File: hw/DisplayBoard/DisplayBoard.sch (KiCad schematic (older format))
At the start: 29 parts, among them J1 Screw_Terminal_01x02, Q1 2N3906, Q2 2N3906, Q3 2N3906, Q4 2N3906, SW1 SW_Push, SW2 SW_Push, SW3 SW_Push, U1 DS1307+, Y1 32.768 KHz

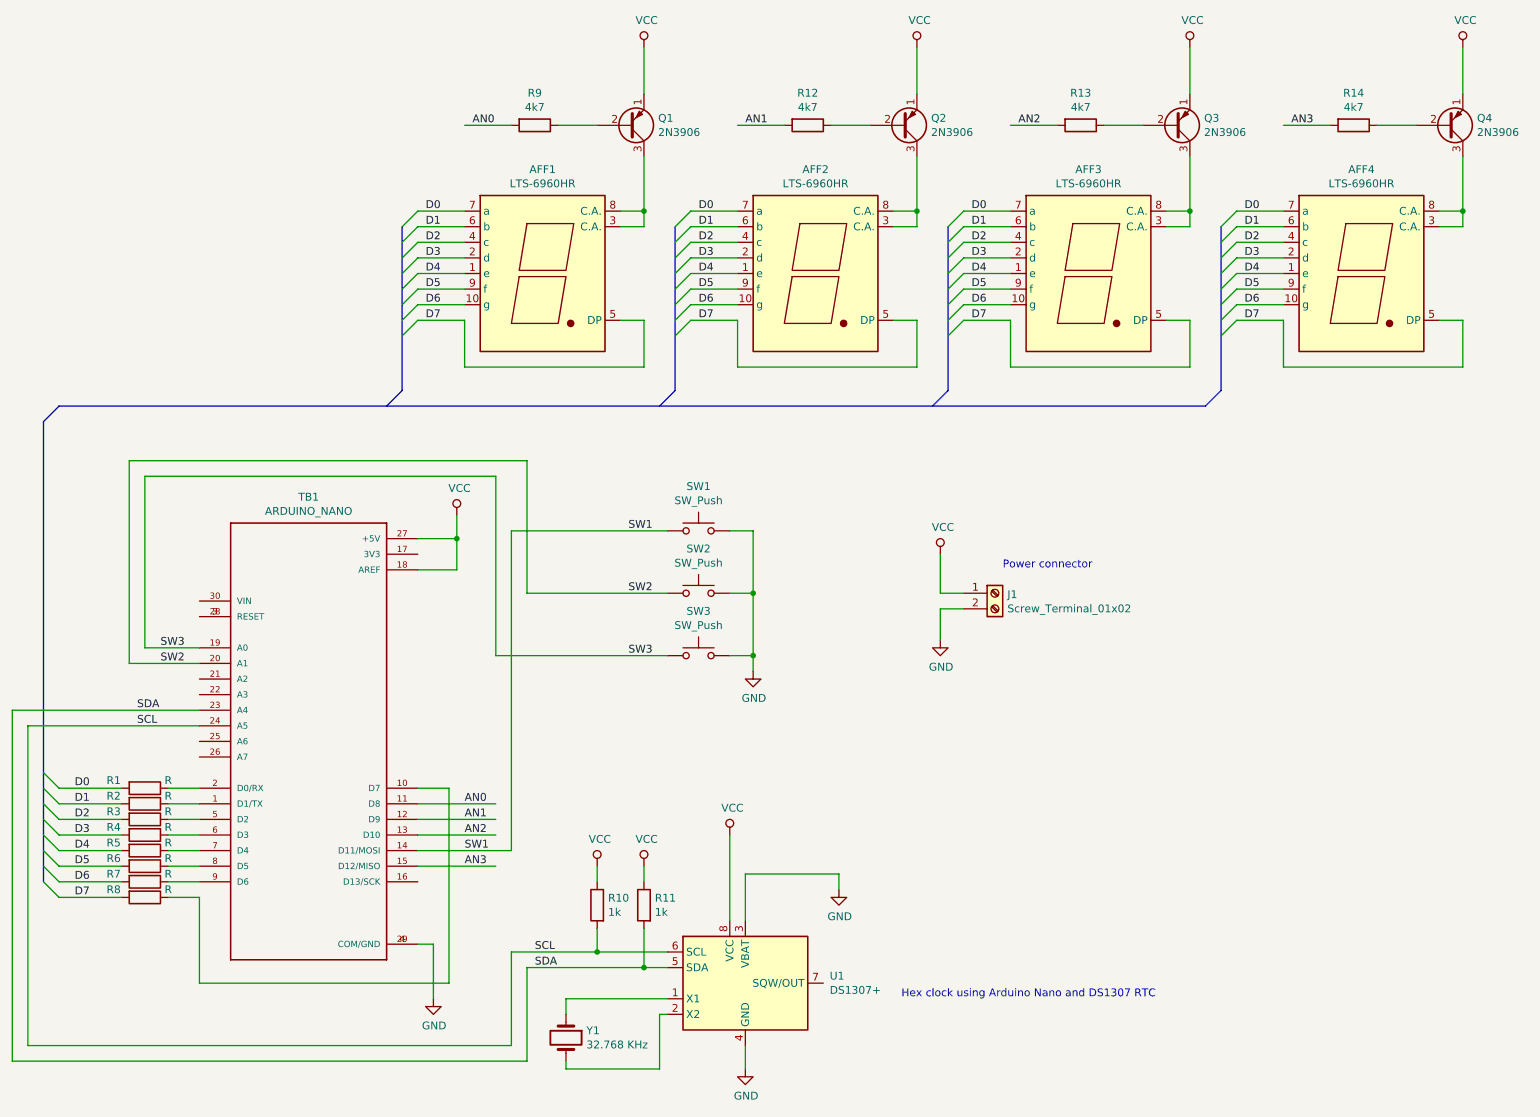
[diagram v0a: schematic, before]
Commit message: edited to make this just the display board
Also, changed to use a 4 digit LED display.
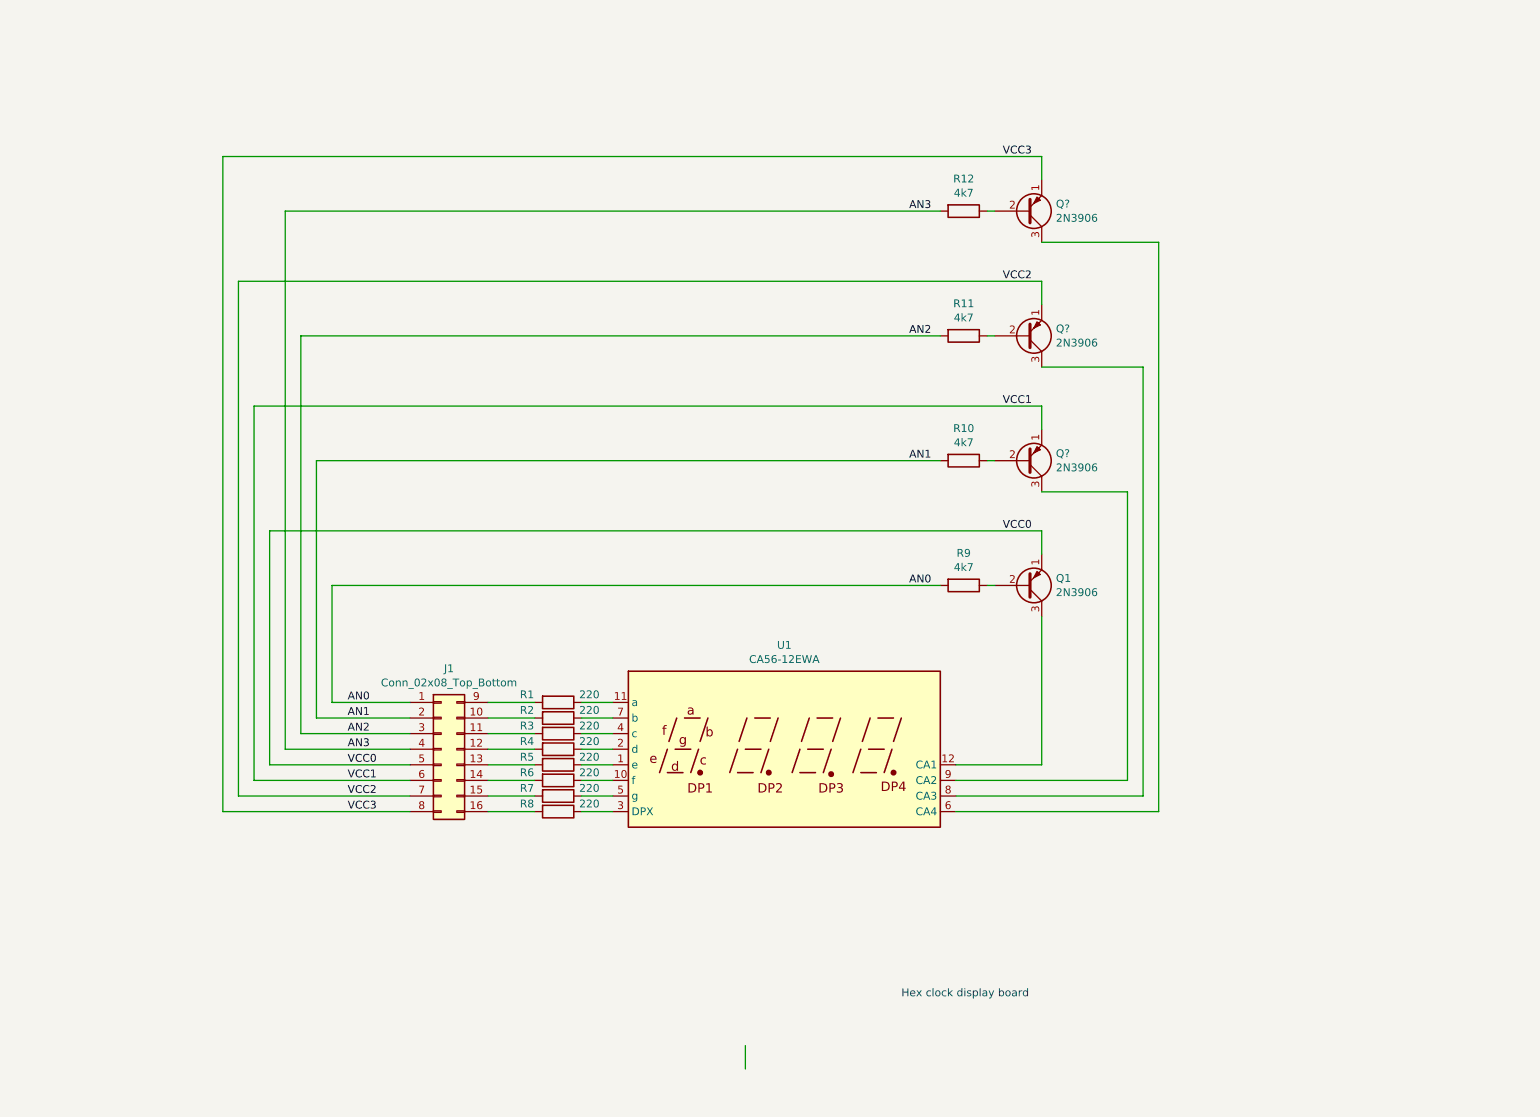
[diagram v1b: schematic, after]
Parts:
- removed AFF1, AFF2, AFF3, AFF4: LTS-6960HR, Display_7Segment:7SegmentLED_LTS6760_LTS6780, symbol Display_Character:LTS-6960HR
- removed J1: Screw_Terminal_01x02, symbol Connector:Screw_Terminal_01x02
- removed Q2, Q3, Q4: 2N3906, symbol device:Q_PNP_EBC
- removed R13, R14: 4k7, symbol device:R
- removed SW1, SW2, SW3: SW_Push, symbol Switch:SW_Push
- removed TB1: ARDUINO_NANO, SHIELD_ARDUINO_NANO, symbol ARDUINO_NANO:ARDUINO_NANO
- removed U1: DS1307+, Package_DIP:DIP-8_W7.62mm, symbol Timer_RTC:DS1307+
- removed Y1: 32.768 KHz, symbol device:Crystal
- added J1: Conn_02x08_Top_Bottom, symbol Connector_Generic:Conn_02x08_Top_Bottom
- added Q? (x3): 2N3906, symbol device:Q_PNP_EBC
- added U1: CA56-12EWA, Display_7Segment:CA56-12EWA, symbol Display_Character:CA56-12EWA
- R1, R2, R3, R4, R5, R6, R7, R8: value R -> 220
- R10, R11: value 1k -> 4k7
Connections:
- net labels added: VCC0, VCC1, VCC2, VCC3
- net labels removed: D0, D1, D2, D3, D4, D5, D6, D7, GND, SCL, SDA, SW1, SW2, SW3, VCC
- wire segments 156 -> 60
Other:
- note added: "Hex clock display board"
- note removed: "Hex clock using Arduino Nano and DS1307 RTC"
- note removed: "Power connector"
- moved on the sheet: Q1, R1, R2, R3, R4, R5, R6, R7, R8, R9

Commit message: generated netlist
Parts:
- gave numbers to parts that had none: 3
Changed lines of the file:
@@
 $EndComp
 $Comp
-L device:Q_PNP_EBC Q?
+L device:Q_PNP_EBC Q4
 U 1 1 5CD9C39D
 P 7150 3500
-F 0 "Q?" H 7341 3454 50  0000 L CNN
+F 0 "Q4" H 7341 3454 50  0000 L CNN
 F 1 "2N3906" H 7341 3545 50  0000 L CNN
 F 2 "" H 7350 3600 50  0001 C CNN
@@
 	7250 3300 7250 3150
 $Comp
-L device:Q_PNP_EBC Q?
+L device:Q_PNP_EBC Q3
 U 1 1 5CD9F12A
 P 7150 2700
-F 0 "Q?" H 7341 2654 50  0000 L CNN
+F 0 "Q3" H 7341 2654 50  0000 L CNN
 F 1 "2N3906" H 7341 2745 50  0000 L CNN
 F 2 "" H 7350 2800 50  0001 C CNN
@@
 	7250 2500 7250 2350
 $Comp
-L device:Q_PNP_EBC Q?
+L device:Q_PNP_EBC Q2
 U 1 1 5CD9F140
 P 7150 1900
-F 0 "Q?" H 7341 1854 50  0000 L CNN
+F 0 "Q2" H 7341 1854 50  0000 L CNN
 F 1 "2N3906" H 7341 1945 50  0000 L CNN
 F 2 "" H 7350 2000 50  0001 C CNN

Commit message: choose component footprints
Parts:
- J1: footprint (none) -> Pin_Headers:Pin_Header_Straight_2x08_Pitch2.54mm
- Q1, Q2, Q3, Q4: footprint (none) -> TO_SOT_Packages_THT:TO-92_Inline_Narrow_Oval
- R1, R10, R11, R12, R2, R3, R4, R5, R6, R7, R8, R9: footprint (none) -> Resistors_ThroughHole:R_Axial_DIN0207_L6.3mm_D2.5mm_P7.62mm_Horizontal
- U1: footprint Display_7Segment:CA56-12EWA -> Displays_7-Segment:CA56-12EWA
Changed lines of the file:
@@
 F 0 "Q1" H 7341 4254 50  0000 L CNN
 F 1 "2N3906" H 7341 4345 50  0000 L CNN
-F 2 "" H 7350 4400 50  0001 C CNN
+F 2 "TO_SOT_Packages_THT:TO-92_Inline_Narrow_Oval" H 7350 4400 50  0001 C CNN
 F 3 "" H 7150 4300 50  0001 C CNN
 	1    7150 4300
@@
 F 0 "R9" V 6543 4300 50  0000 C CNN
 F 1 "4k7" V 6634 4300 50  0000 C CNN
-F 2 "" V 6680 4300 50  0001 C CNN
+F 2 "Resistors_ThroughHole:R_Axial_DIN0207_L6.3mm_D2.5mm_P7.62mm_Horizontal" V 6680 4300 50  0001 C CNN
 F 3 "" H 6750 4300 50  0001 C CNN
 	1    6750 4300
@@
 F 0 "R1" V 4100 4850 50  0000 C CNN
 F 1 "220" V 4100 5250 50  0000 C CNN
-F 2 "" V 4080 5050 50  0001 C CNN
+F 2 "Resistors_ThroughHole:R_Axial_DIN0207_L6.3mm_D2.5mm_P7.62mm_Horizontal" V 4080 5050 50  0001 C CNN
 F 3 "" H 4150 5050 50  0001 C CNN
 	1    4150 5050
@@
 F 0 "R2" V 4100 4950 50  0000 C CNN
 F 1 "220" V 4100 5350 50  0000 C CNN
-F 2 "" V 4080 5150 50  0001 C CNN
+F 2 "Resistors_ThroughHole:R_Axial_DIN0207_L6.3mm_D2.5mm_P7.62mm_Horizontal" V 4080 5150 50  0001 C CNN
 F 3 "" H 4150 5150 50  0001 C CNN
 	1    4150 5150
@@
 F 0 "R3" V 4100 5050 50  0000 C CNN
 F 1 "220" V 4100 5450 50  0000 C CNN
-F 2 "" V 4080 5250 50  0001 C CNN
+F 2 "Resistors_ThroughHole:R_Axial_DIN0207_L6.3mm_D2.5mm_P7.62mm_Horizontal" V 4080 5250 50  0001 C CNN
 F 3 "" H 4150 5250 50  0001 C CNN
 	1    4150 5250
@@
 F 0 "R4" V 4100 5150 50  0000 C CNN
 F 1 "220" V 4100 5550 50  0000 C CNN
-F 2 "" V 4080 5350 50  0001 C CNN
+F 2 "Resistors_ThroughHole:R_Axial_DIN0207_L6.3mm_D2.5mm_P7.62mm_Horizontal" V 4080 5350 50  0001 C CNN
 F 3 "" H 4150 5350 50  0001 C CNN
 	1    4150 5350
@@
 F 0 "R5" V 4100 5250 50  0000 C CNN
 F 1 "220" V 4100 5650 50  0000 C CNN
-F 2 "" V 4080 5450 50  0001 C CNN
+F 2 "Resistors_ThroughHole:R_Axial_DIN0207_L6.3mm_D2.5mm_P7.62mm_Horizontal" V 4080 5450 50  0001 C CNN
 F 3 "" H 4150 5450 50  0001 C CNN
 	1    4150 5450
@@
 F 0 "R6" V 4100 5350 50  0000 C CNN
 F 1 "220" V 4100 5750 50  0000 C CNN
-F 2 "" V 4080 5550 50  0001 C CNN
+F 2 "Resistors_ThroughHole:R_Axial_DIN0207_L6.3mm_D2.5mm_P7.62mm_Horizontal" V 4080 5550 50  0001 C CNN
 F 3 "" H 4150 5550 50  0001 C CNN
 	1    4150 5550
@@
 F 0 "R7" V 4100 5450 50  0000 C CNN
 F 1 "220" V 4100 5850 50  0000 C CNN
-F 2 "" V 4080 5650 50  0001 C CNN
+F 2 "Resistors_ThroughHole:R_Axial_DIN0207_L6.3mm_D2.5mm_P7.62mm_Horizontal" V 4080 5650 50  0001 C CNN
 F 3 "" H 4150 5650 50  0001 C CNN
 	1    4150 5650
@@
 F 0 "R8" V 4100 5550 50  0000 C CNN
 F 1 "220" V 4100 5950 50  0000 C CNN
-F 2 "" V 4080 5750 50  0001 C CNN
+F 2 "Resistors_ThroughHole:R_Axial_DIN0207_L6.3mm_D2.5mm_P7.62mm_Horizontal" V 4080 5750 50  0001 C CNN
 F 3 "" H 4150 5750 50  0001 C CNN
 	1    4150 5750
@@
 F 0 "U1" H 5600 6017 50  0000 C CNN
 F 1 "CA56-12EWA" H 5600 5926 50  0000 C CNN
-F 2 "Display_7Segment:CA56-12EWA" H 5600 4750 50  0001 C CNN
+F 2 "Displays_7-Segment:CA56-12EWA" H 5600 4750 50  0001 C CNN
 F 3 "" H 5170 5380 50  0001 C CNN
 	1    5600 5350
@@
 F 0 "Q4" H 7341 3454 50  0000 L CNN
 F 1 "2N3906" H 7341 3545 50  0000 L CNN
-F 2 "" H 7350 3600 50  0001 C CNN
+F 2 "TO_SOT_Packages_THT:TO-92_Inline_Narrow_Oval" H 7350 3600 50  0001 C CNN
 F 3 "" H 7150 3500 50  0001 C CNN
 	1    7150 3500
@@
 F 0 "R10" V 6543 3500 50  0000 C CNN
 F 1 "4k7" V 6634 3500 50  0000 C CNN
-F 2 "" V 6680 3500 50  0001 C CNN
+F 2 "Resistors_ThroughHole:R_Axial_DIN0207_L6.3mm_D2.5mm_P7.62mm_Horizontal" V 6680 3500 50  0001 C CNN
 F 3 "" H 6750 3500 50  0001 C CNN
 	1    6750 3500
@@
 F 0 "Q3" H 7341 2654 50  0000 L CNN
 F 1 "2N3906" H 7341 2745 50  0000 L CNN
-F 2 "" H 7350 2800 50  0001 C CNN
+F 2 "TO_SOT_Packages_THT:TO-92_Inline_Narrow_Oval" H 7350 2800 50  0001 C CNN
 F 3 "" H 7150 2700 50  0001 C CNN
 	1    7150 2700
@@
 F 0 "R11" V 6543 2700 50  0000 C CNN
 F 1 "4k7" V 6634 2700 50  0000 C CNN
-F 2 "" V 6680 2700 50  0001 C CNN
+F 2 "Resistors_ThroughHole:R_Axial_DIN0207_L6.3mm_D2.5mm_P7.62mm_Horizontal" V 6680 2700 50  0001 C CNN
 F 3 "" H 6750 2700 50  0001 C CNN
 	1    6750 2700
@@
 F 0 "Q2" H 7341 1854 50  0000 L CNN
 F 1 "2N3906" H 7341 1945 50  0000 L CNN
-F 2 "" H 7350 2000 50  0001 C CNN
+F 2 "TO_SOT_Packages_THT:TO-92_Inline_Narrow_Oval" H 7350 2000 50  0001 C CNN
 F 3 "" H 7150 1900 50  0001 C CNN
 	1    7150 1900
@@
 F 0 "R12" V 6543 1900 50  0000 C CNN
 F 1 "4k7" V 6634 1900 50  0000 C CNN
-F 2 "" V 6680 1900 50  0001 C CNN
+F 2 "Resistors_ThroughHole:R_Axial_DIN0207_L6.3mm_D2.5mm_P7.62mm_Horizontal" V 6680 1900 50  0001 C CNN
 F 3 "" H 6750 1900 50  0001 C CNN
 	1    6750 1900
@@
 F 0 "J1" H 3450 5867 50  0000 C CNN
 F 1 "Conn_02x08_Top_Bottom" H 3450 5776 50  0000 C CNN
-F 2 "" H 3400 5350 50  0001 C CNN
+F 2 "Pin_Headers:Pin_Header_Straight_2x08_Pitch2.54mm" H 3400 5350 50  0001 C CNN
 F 3 "~" H 3400 5350 50  0001 C CNN
 	1    3400 5350

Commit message: working on PCB layout
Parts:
- removed J1: Conn_02x08_Top_Bottom, Pin_Headers:Pin_Header_Straight_2x08_Pitch2.54mm, symbol Connector_Generic:Conn_02x08_Top_Bottom
- added J1: Conn_02x08_Odd_Even, Pin_Headers:Pin_Header_Straight_2x08_Pitch2.54mm, symbol Connector_Generic:Conn_02x08_Odd_Even
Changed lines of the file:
@@
 Text Label 7000 1550 0    50   ~ 0
 VCC3
-$Comp
-L Connector_Generic:Conn_02x08_Top_Bottom J1
-U 1 1 5CDBD573
-P 3400 5350
-F 0 "J1" H 3450 5867 50  0000 C CNN
-F 1 "Conn_02x08_Top_Bottom" H 3450 5776 50  0000 C CNN
-F 2 "Pin_Headers:Pin_Header_Straight_2x08_Pitch2.54mm" H 3400 5350 50  0001 C CNN
-F 3 "~" H 3400 5350 50  0001 C CNN
-	1    3400 5350
-	1    0    0    -1
-$EndComp
 Wire Wire Line
 	4000 5050 3700 5050
@@
 Wire Wire Line
 	2000 5750 3200 5750
+$Comp
+L Connector_Generic:Conn_02x08_Odd_Even J1
+U 1 1 5CD74093
+P 3400 5350
+F 0 "J1" H 3450 5867 50  0000 C CNN
+F 1 "Conn_02x08_Odd_Even" H 3450 5776 50  0000 C CNN
+F 2 "Pin_Headers:Pin_Header_Straight_2x08_Pitch2.54mm" H 3400 5350 50  0001 C CNN
+F 3 "~" H 3400 5350 50  0001 C CNN
+	1    3400 5350
+	1    0    0    -1
+$EndComp
 $EndSCHEMATC
